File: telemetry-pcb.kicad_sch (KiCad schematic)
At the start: 22 parts, among them CN1 12V, CN8 GPS, M1 MountingHole, M2 MountingHole, M3 MountingHole, M4 MountingHole, T1 TEST_12V, T2 GPIO_L, T3 GPIO_R, T4 TEST_3V3

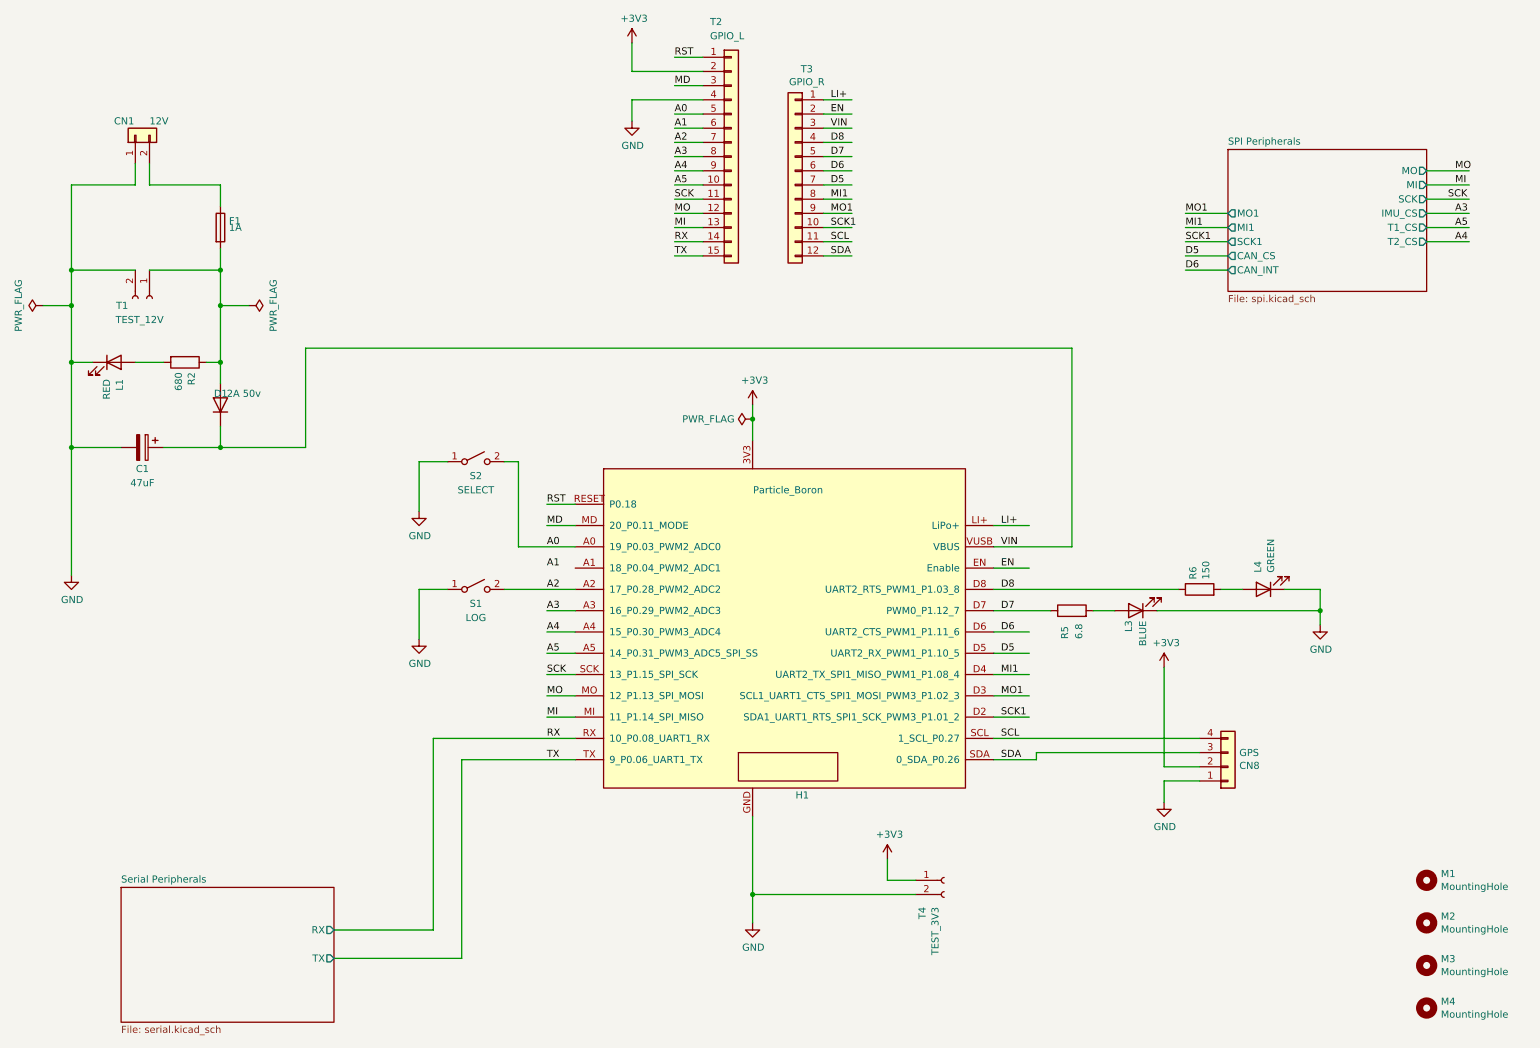
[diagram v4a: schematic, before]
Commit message: Completed PCB routing
new footprints added to Footprints folder, added I2C peripherals page.
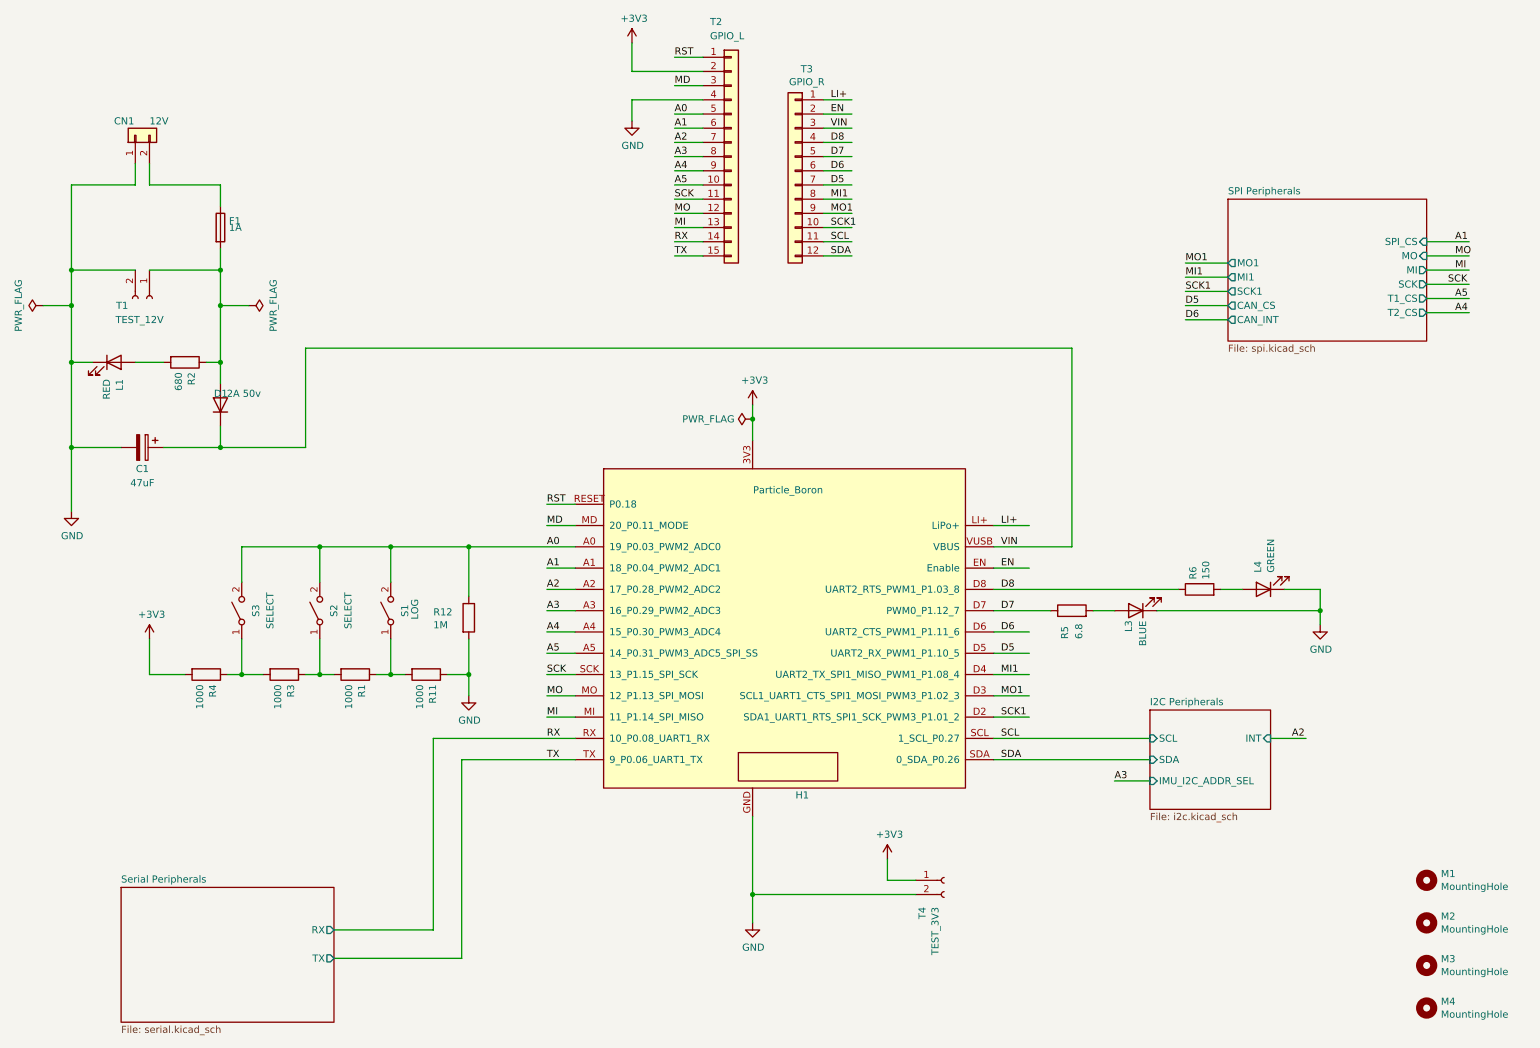
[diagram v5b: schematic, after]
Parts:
- removed CN8: GPS, Connector_JST:JST_GH_SM04B-GHS-TB_1x04-1MP_P1.25mm_Horizontal, symbol Connector_Generic:Conn_01x04
- added R1, R11, R3, R4: 1000, Resistor_SMD:R_0805_2012Metric, symbol Device:R
- added R12: 1M, Resistor_SMD:R_0805_2012Metric, symbol Device:R
- added S3: SELECT, Button_Switch_THT:SW_PUSH_6mm_H13mm, symbol Switch:SW_SPST
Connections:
- net +3V3: now also R4.2
- net A0: now also S1.2 (B), R12.1, S3.2 (B)
- net A1: now also H1.A1 (18_P0.04_PWM2_ADC1)
- net A2: no longer S1.2 (B)
- net GND: now also R11.1, R12.2; no longer S1.1 (A), S2.1 (A)
- new net: R1.2, R3.1, S2.1 (A)
- new net: R3.2, R4.1, S3.1 (A)
- new net: R1.1, R11.2, S1.1 (A)
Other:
- added sheet I2C Peripherals (i2c.kicad_sch)
- sheet SPI Peripherals ports: added SPI_CS; removed IMU_CS

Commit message: Backup
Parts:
- S2: value SELECT -> SELECT2
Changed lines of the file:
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@@
 			)
 		)
-		(property "Value" "SELECT"
+		(property "Value" "SELECT2"
 			(at 71.12 114.3 0)
 			(effects

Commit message: more changes
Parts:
- removed CN1: 12V, telemetry-pcb:molex_sl_1x02_horizontal, symbol Connector_Generic:Conn_01x02
- added J6: 436500201, Footprints:CONN_SD-43650-001_02_MOL, symbol telemetry_3.0_sch_library:436500201
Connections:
- net GND: now also J6.1
- net at F1.1: now also J6.2
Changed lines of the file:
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@@
-	)
-	(symbol
-		(lib_id "Connector_Generic:Conn_01x02")
-		(at 33.02 29.21 90)
-		(unit 1)
-		(exclude_from_sim no)
-		(in_bom yes)
-		(on_board yes)
-		(dnp no)
-		(property "Reference" "CN1"
-			(at 29.21 26.67 90)
-			(effects
-				(font
-					(size 1.27 1.27)
-				)
-				(justify right)
-			)
-		)
-		(property "Value" "12V"
-			(at 35.56 26.67 90)
-			(effects
-				(font
-					(size 1.27 1.27)
-				)
-				(justify right)
-			)
-		)
-		(property "Footprint" "telemetry-pcb:molex_sl_1x02_horizontal"
-			(at 33.02 29.21 0)
-			(effects
-				(font
-					(size 1.27 1.27)
-				)
-				(hide yes)
-			)
-		)
-		(property "Datasheet" "~"
-			(at 33.02 29.21 0)
-			(effects
-				(font
-					(size 1.27 1.27)
-				)
-				(hide yes)
-			)
-		)
-		(property "Description" ""
-			(at 33.02 29.21 0)
-			(effects
-				(font
-					(size 1.27 1.27)
-				)
-			)
-		)
-		(pin "1"
-		)
-		(pin "2"
-		)
-		(instances
-			(project "telemetry-pcb"
-				(path "/871fe08d-2afd-493a-a8ef-c8aa2cbbb7b9"
-					(reference "CN1")
-					(unit 1)
-				)
-			)
-		)
 	)
 	(symbol
@@
 					(unit 1)
 				)
+			)
+		)
+	)
+	(symbol
+		(lib_id "telemetry_3.0_sch_library:436500201")
+		(at 33.02 34.29 90)
+		(unit 1)
+		(exclude_from_sim no)
+		(in_bom yes)
+		(on_board yes)
+		(dnp no)
+		(fields_autoplaced yes)
+		(property "Reference" "J6"
+			(at 39.37 24.1299 90)
+			(effects
+				(font
+					(size 1.27 1.27)
+				)
+				(justify right)
+			)
+		)
+		(property "Value" "436500201"
+			(at 39.37 26.6699 90)
+			(effects
+				(font
+					(size 1.27 1.27)
+				)
+				(justify right)
+			)
+		)
+		(property "Footprint" "Footprints:CONN_SD-43650-001_02_MOL"
+			(at 33.02 34.29 0)
+			(effects
+				(font
+					(size 1.27 1.27)
+				)
+				(justify bottom)
+				(hide yes)
+			)
+		)
+		(property "Datasheet" ""
+			(at 33.02 34.29 0)
+			(effects
+				(font
+					(size 1.27 1.27)
+				)
+				(hide yes)
+			)
+		)
+		(property "Description" ""
+			(at 33.02 34.29 0)
+			(effects
+				(font
+					(size 1.27 1.27)
+				)
+				(hide yes)
+			)
+		)
+		(property "MFR_NAME" "Molex Connector Corporation"
+			(at 33.02 34.29 0)
+			(effects
+				(font
+					(size 1.27 1.27)
+				)
+				(justify bottom)
+				(hide yes)
+			)
+		)
+		(property "MANUFACTURER_PART_NUMBER" "436500201"
+			(at 33.02 34.29 0)
+			(effects
+				(font
+					(size 1.27 1.27)
+				)
+				(justify bottom)
+				(hide yes)
+			)
+		)
+		(pin "1"
+		)
+		(pin "2"
+		)
+		(instances
+			(project ""
+				(path "/871fe08d-2afd-493a-a8ef-c8aa2cbbb7b9"
+					(reference "J6")
+					(unit 1)
+				)
